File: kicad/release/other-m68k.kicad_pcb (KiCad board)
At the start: 4 copper layers, 180 x 125 mm, 151 parts, among them J1 USB-C power, J10 S-video, J11 FTDI B (GND CTS VCC TXD RXD R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, J2 FTDI (GND CTS VCC TXD RXD RTS), J3 PS/2, J4 microSD DM3AT-SF-PEJM5, J5 RCA composite, J6 3.5mm audio, J7 JTAG (ByteBlaster), J9 Logic analyzer (gusmanb 2x15), SW1 RESET, SW2 NMI, U1 MC68000P12, U10 MC68681P, U11 AD724JR, U12 AP2112K-3.3, U13 MCP130T-450I/TT, U2 AS6C4008-55PCN (upper, D15..D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, U3 AS6C4008-55PCN (lower, D7..D0), U4 SST39SF040-70 (even, D15..D8), U5 SST39SF040-70 (odd, D7..D0), U6 ATF1508AS-7JX84 (MMU), U7 ATF1508AS-7JX84 (I/O), U8 74AHCT245 (hi), U9 74AHCT245 (lo), X1 24MHz, Y1 3.6864MHz, Y2 3.579545MHz

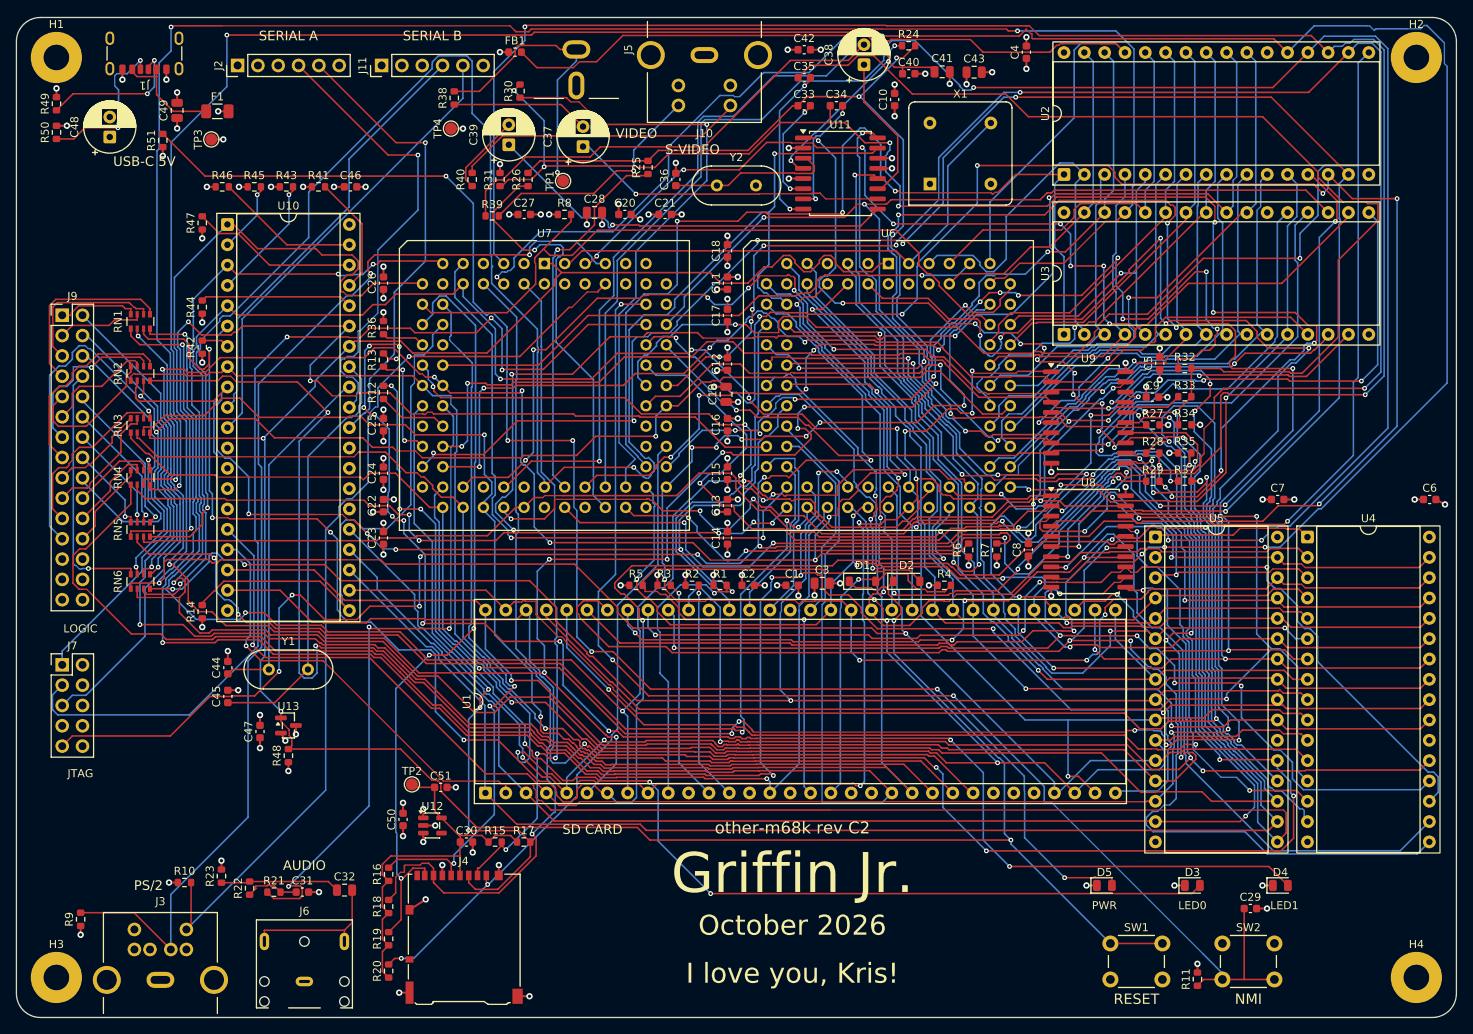
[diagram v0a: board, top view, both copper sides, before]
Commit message: spec rev 11 / board rev C3: Atari joystick and paddle port on the DUART's I/O pins
Hardware: J12, a DE-9 male with the Atari pinout on the front edge. The five switches go
through 1 k into DUART inputs IP0..IP4 (up, down, left, right, fire), which already have
10 k pull-ups. Paddles: each pot charges, through 1 k, a 15 nF capacitor; a 74HC14 gate
(U14) pulls the up (A) or down (B) line low through a BAT54W when the capacitor passes its
threshold, so those lines double as end-of-charge signals (a joystick has no pots, paddles
no up/down switches); a dual NPN (Q1) on OP0 shorts both capacitors (pin high = shorted,
the reset state); +5 V through a 200 mA polyfuse. Paddle A's button is on pin 4 (right),
B's on pin 3 (left). The dedication moved under the SRAMs to make room. Routed with the
optimizer off: 0 DRC violations, 0 unrouted; fab package and release regenerated; the six
new part numbers are flagged verify in parts.json.

Firmware (fw/joy.c): sys_joystick (40) returns the JOY_* mask from one input-port read.
sys_paddles (41) fills struct paddles {a, b 0..1023 (1023 = 12 ms = 2764 counts), valid
bits, frame}: the first call starts measuring, NULL or program exit stops it. The
counter/timer runs free in timer mode from X1/16 (230.4 kHz) and IP0/IP1 change
interrupts are enabled (ACR 0x73, IMR.IPC). Each frame the VBLANK handler shorts the
capacitors; when the DUART reports the lines rising (its 38.4 kHz sampler has seen the
step) the level-3 handler releases them and notes the counter, and it timestamps each
fall; if nothing rose the next VBLANK releases directly. Measured in the emulator: 0.2 %
of the CPU with no paddle, 1.8 % with two. A joystick held up/down while measuring reads
as no paddle; a program using the counter/timer itself must not use paddles.

Spec: joystick section, DUART IPCR/ACR/IP/OPR fields, syscalls 40-41, struct paddles,
JOY_*/PADDLE_* constants. Emulator: joy.c models the port (--joy switches, --paddle A,B
or a game controller's triggers, SD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
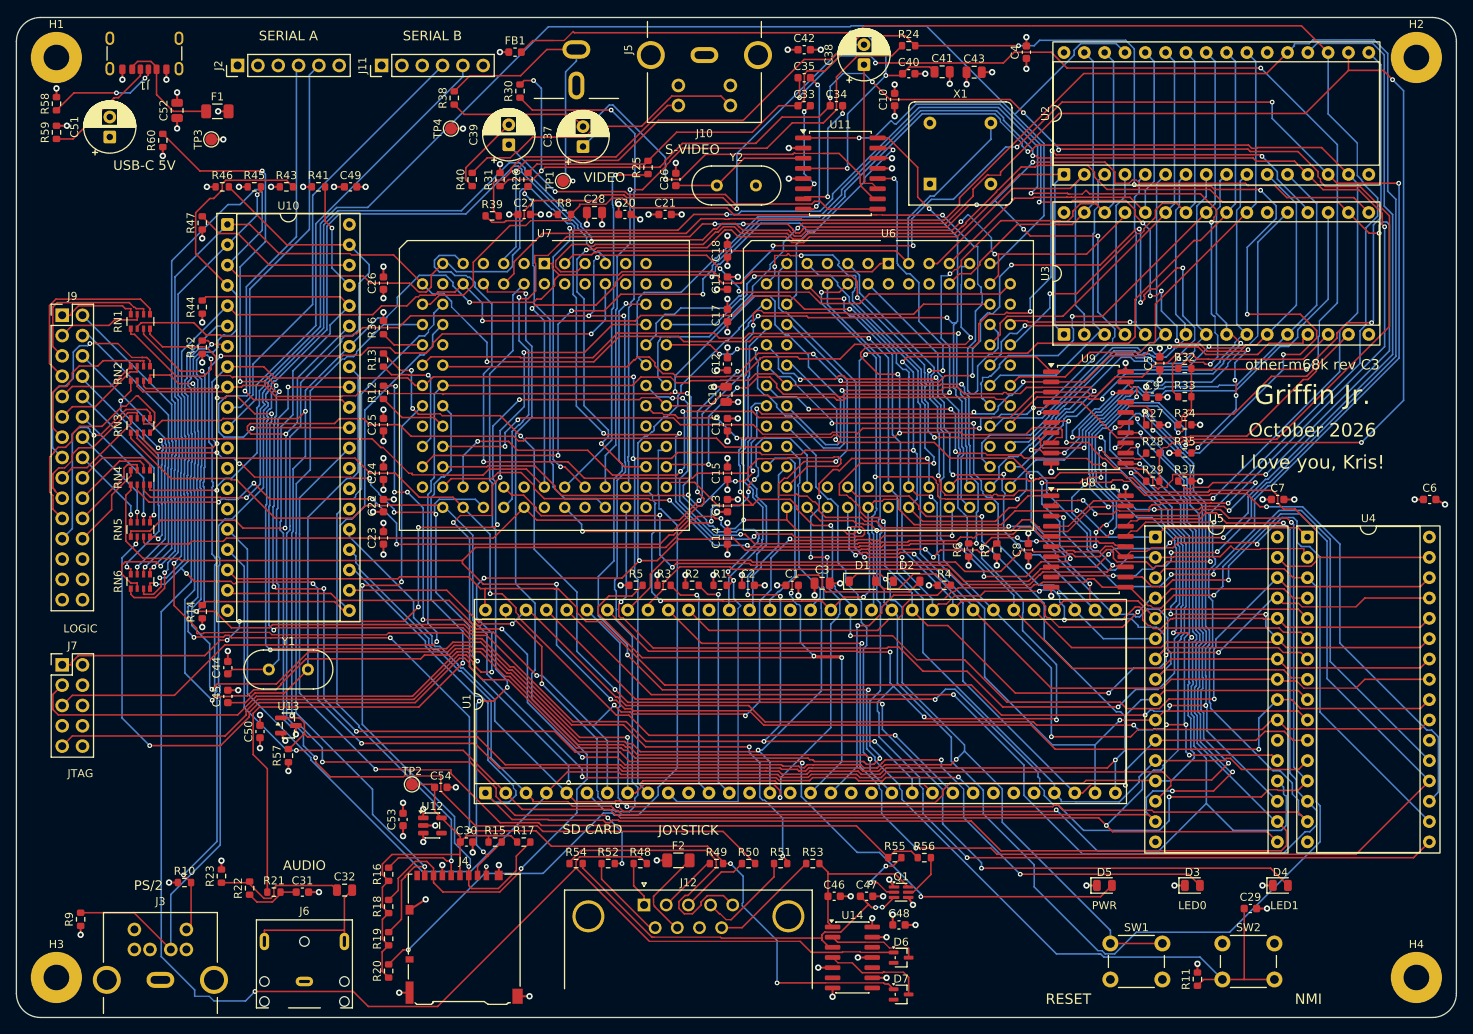
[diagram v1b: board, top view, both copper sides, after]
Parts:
- added C52: 10uF, C_0805_2012Metric, F.Cu at (20.1, 11.6)
- added C53: 1uF, C_0603_1608Metric, F.Cu at (48.3, 100.2)
- added C54: 1uF, C_0603_1608Metric, F.Cu at (53.0, 96.2)
- added D6: BAT54W, SOT-323_SC-70, F.Cu at (110.6, 117.5)
- added D7: BAT54W, SOT-323_SC-70, F.Cu at (110.6, 122.1)
- added F2: 200mA, Fuse_1206_3216Metric, F.Cu at (82.8, 105.4)
- added J12: Joystick (Atari DE-9), DSUB-9_Pins_Horizontal_P2.77x2.84mm_EdgePinOffset7.70mm_Housed_MountingHolesOffset9.12mm, F.Cu at (78.5, 110.9)
- added Q1: MMDT3904, SOT-363_SC-70-6, F.Cu at (110.6, 109.3)
- added R52: 1k, R_0603_1608Metric, F.Cu at (74.0, 105.8)
- added R53: 1k, R_0603_1608Metric, F.Cu at (99.5, 105.8)
- added R54: 1k, R_0603_1608Metric, F.Cu at (70.0, 105.8)
- added R55: 4.7k, R_0603_1608Metric, F.Cu at (109.8, 105.0)
- added R56: 4.7k, R_0603_1608Metric, F.Cu at (113.5, 105.0)
- added R57: 10k, R_0603_1608Metric, F.Cu at (34.0, 92.3)
- added R58: 5.1k, R_0603_1608Metric, F.Cu at (5.01, 10.8)
- added R59: 5.1k, R_0603_1608Metric, F.Cu at (5.01, 14.4)
- added R60: 1k, R_0603_1608Metric, F.Cu at (18.3, 15.4)
- added U14: 74HC14, SOIC-14_3.9x8.7mm_P1.27mm, F.Cu at (104.5, 117.5)
- C46, C47: value 100nF -> 15nF
- C48: value 100uF -> 100nF; footprint CP_Radial_D6.3mm_P2.50mm -> C_0603_1608Metric
- C49: value 10uF -> 100nF; footprint C_0805_2012Metric -> C_0603_1608Metric
- C50: value 1uF -> 100nF
- C51: value 1uF -> 100uF; footprint C_0603_1608Metric -> CP_Radial_D6.3mm_P2.50mm
- R48: value 10k -> 1k
- R49, R50: value 5.1k -> 1k
- moved C48 139.4 mm to (110.3, 113.4), turned to 0 degrees
- moved R50 125.8 mm to (91.5, 105.8), turned to 0 degrees
- moved R49 125.8 mm to (87.5, 105.8), turned to 0 degrees
- moved R51 118.9 mm to (95.5, 105.8), turned to 0 degrees
- moved C46 107.3 mm to (102.2, 109.8)
- moved C51 91.2 mm to (11.7, 14.9), turned to 90 degrees
- moved C47 78.6 mm to (106.3, 109.8), turned to 0 degrees
- moved R48 46.0 mm to (78.0, 105.8), turned to 0 degrees
- moved C49 23.7 mm to (41.8, 21.2), turned to 0 degrees
- moved C50 21.0 mm to (30.4, 89.3)
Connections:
- C46 pad 1: VCC -> JOY_POTA_C
- C47 pad 1: VCC -> JOY_POTB_C
- C51 pad 1: +3V3 -> VCC
- R48 pad 1: VCC -> JOY_UP
- R48 pad 2: SYSRESET -> DUART_IP0
- R49 pad 1: CC1 -> JOY_DOWN
- R49 pad 2: GND -> DUART_IP1
- R50 pad 1: CC2 -> JOY_LEFT
- R50 pad 2: GND -> DUART_IP2
- R51 pad 1: VCC -> JOY_RIGHT
- R51 pad 2: PWRLED_A -> DUART_IP3
- U10 pad 29: unconnected-(U10-OP0-Pad29) -> DUART_OP0
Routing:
- net DUART_IP0: track 3.45 -> 201.3 mm, vias 0 -> 2
- net DUART_IP1: track 15.7 -> 194.7 mm, vias 1 -> 5
- net DUART_IP3: track 8.98 -> 153.9 mm, vias 1 -> 4
- net DUART_IP2: track 19.0 -> 143.3 mm, vias 0 -> 1
- net DUART_OP0: track 0.00 -> 119.9 mm, vias 0 -> 1
- net DUART_IP4: track 18.1 -> 137.4 mm, vias 0 -> 3
- net A6: track 187.5 -> 100.5 mm, vias 8 -> 4
- net VSYNC: track 235.9 -> 155.8 mm, vias 3 -> 5
- net A10: track 182.7 -> 104.9 mm, vias 7 -> 0
- net MD14: track 256.4 -> 181.1 mm
- net G2: track 183.8 -> 115.7 mm, vias 7 -> 8
- net A16: track 121.2 -> 185.2 mm, vias 4 -> 0
- net D14: track 130.9 -> 189.9 mm, vias 6 -> 3
- net WEL: track 226.7 -> 172.8 mm, vias 3 -> 4
- net R_DAC: track 127.1 -> 180.0 mm, vias 3 -> 6
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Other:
- board text added: "JOYSTICK"
- board text added: "other-m68k rev C3"
- board text removed: "other-m68k rev C2"

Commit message: spec rev 12 / board rev C3: serial header B powers its device; OP1 on its RTS pin
J11 pin 3 carries 5 V through F3 (200 mA polyfuse) and D8 (BAT54W, so a 5 V FTDI cable
plugged in there cannot back-feed the board) for the serial-mouse MAX232 adapter; pin 6
(RTS) is DUART OP1 so firmware can switch the mouse's RTS/DTR power and provoke its
identification byte. J2 keeps GND, TXD, RXD only. Routed with the optimizer off after
moving the analyser's resistor arrays 1.5 mm from the header: 0 DRC violations, 0
unrouted; fab package and release regenerated. Spec, KiCad README, ORDER.md, architecture
and the programmer's guide (2.11 channel B) describe it; no firmware change.

Co-Authored-By: Claude Fable 5.1 <noreply@anthropic.com>
Claude-Session: https://claude.ai/code/session_019bbFLKMxhKXGW6aABP44Z1
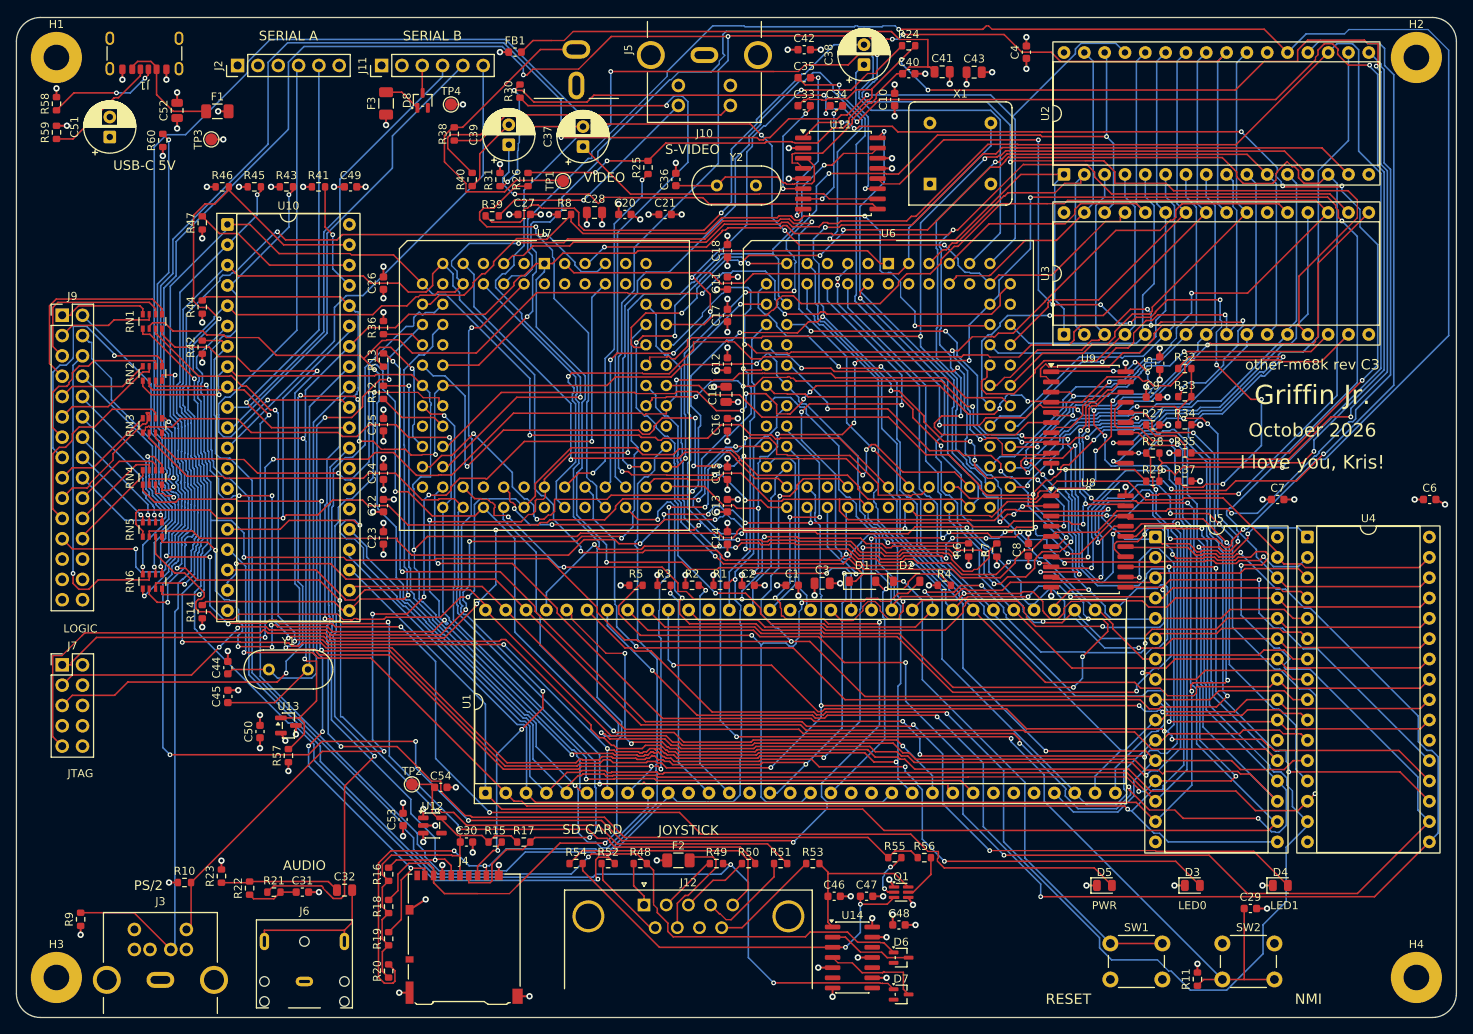
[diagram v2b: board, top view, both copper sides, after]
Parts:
- added D8: BAT54W, SOT-323_SC-70, F.Cu at (50.8, 10.4)
- added F3: 200mA, Fuse_1206_3216Metric, F.Cu at (46.2, 10.7)
- moved R38 4.50 mm to (54.7, 14.6)
- moved TP4 3.02 mm to (54.3, 10.9), turned to 0 degrees
- moved RN1 1.50 mm to (17.0, 38.0)
- moved RN2 1.50 mm to (17.0, 44.5)
- moved RN3 1.50 mm to (17.0, 51.0)
- moved RN4 1.50 mm to (17.0, 57.5)
- moved RN5 1.50 mm to (17.0, 64.0)
- moved RN6 1.50 mm to (17.0, 70.5)
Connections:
- J11 pad 3: unconnected-(J11-Pin_3-Pad3) -> SERB_VCC
- J11 pad 6: unconnected-(J11-Pin_6-Pad6) -> DUART_OP1
- U10 pad 12: unconnected-(U10-OP1-Pad12) -> DUART_OP1
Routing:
- net MD0: track 126.9 -> 242.9 mm, vias 8 -> 4
- net RAMOE: track 201.4 -> 290.9 mm
- net MD12: track 225.6 -> 142.9 mm, vias 7 -> 3
- net BUFEN: track 224.9 -> 152.8 mm, vias 6 -> 8
- net D12: track 137.5 -> 200.4 mm, vias 1 -> 5
- net DUART_OP1: track 0.00 -> 62.3 mm
- net A16: track 185.2 -> 123.3 mm, vias 0 -> 2
- net DUART_IP0: track 201.3 -> 149.4 mm, vias 2 -> 1
- net D14: track 189.9 -> 139.1 mm, vias 3 -> 4
- net LATCH: track 80.9 -> 128.7 mm
- net A2: track 294.4 -> 247.7 mm, vias 8 -> 4
- net MD8: track 186.5 -> 140.1 mm
- net MD4: track 193.0 -> 149.4 mm, vias 4 -> 3
- net MD6: track 152.8 -> 110.2 mm, vias 7 -> 5
- net A14: track 124.9 -> 165.7 mm, vias 4 -> 7
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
